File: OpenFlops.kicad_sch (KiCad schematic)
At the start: 89 parts, among them J99 OSHW_LOGO, P1 FLOPPY_CONN, P2 POWER_INPUT, P3 USB_A_FEMALE, P4 PROG_PORT, P5 JUMPER_JC, P6 ENCODER_PORT, P7 DISPLAY_PORT, P8 USB_HEADER, P9 EXTERNAL_SPEAKER, Q1 BSS138, Q2 BSS138, Q3 BSS138, Q4 BSS138, Q5 BSS138, Q6 BSS138, Q7 MMBT3904, U1 74HCT04, U3 STM32F105RBT6, U4 LM1117-3.3, Y1 8 MHz

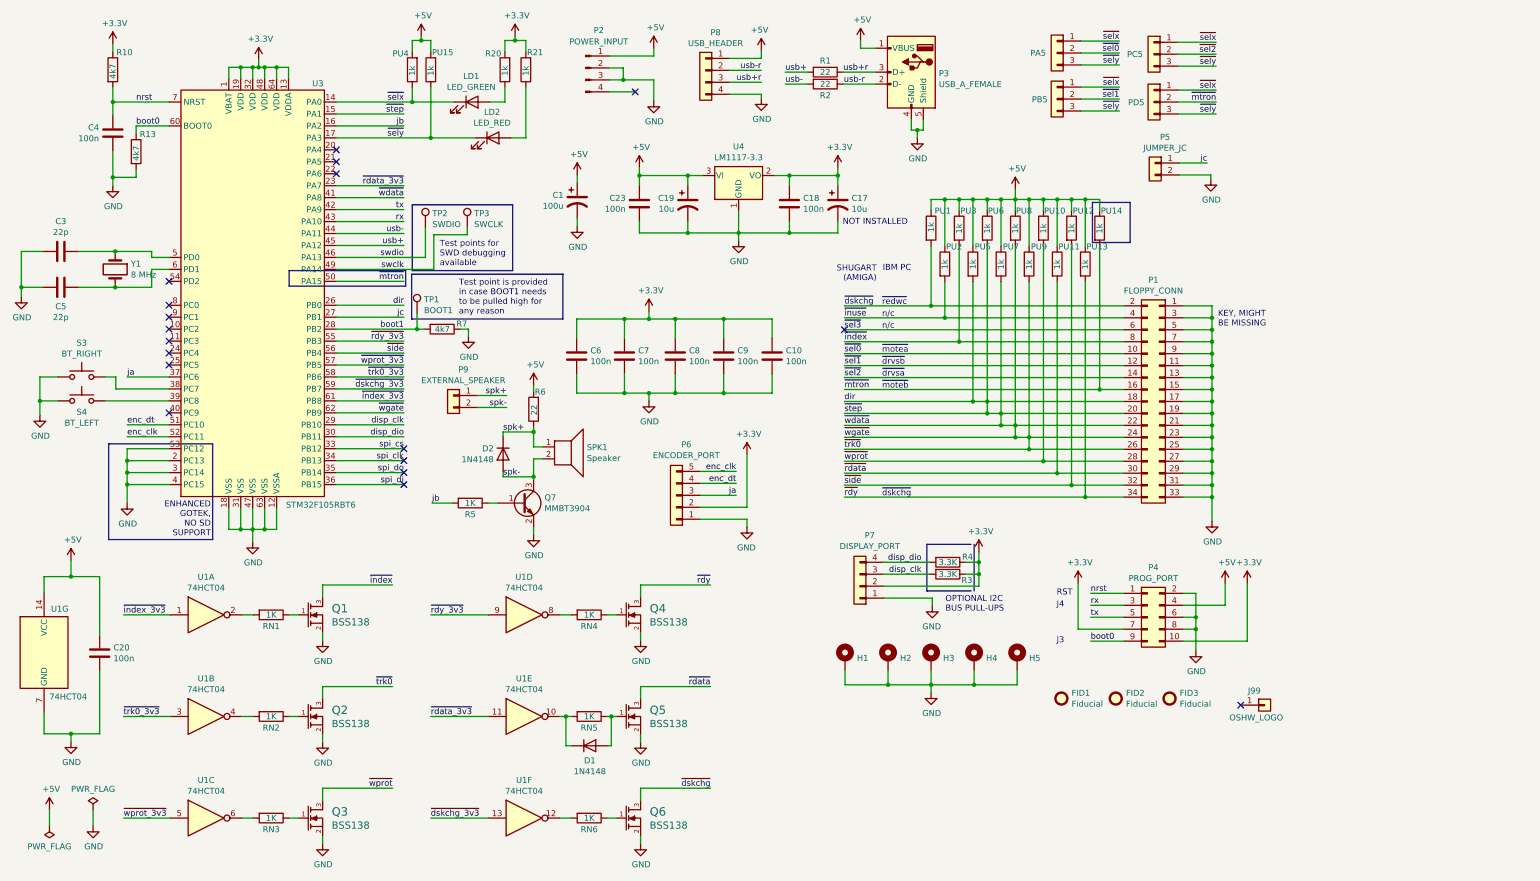
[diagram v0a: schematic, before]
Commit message: update for citizen w1d
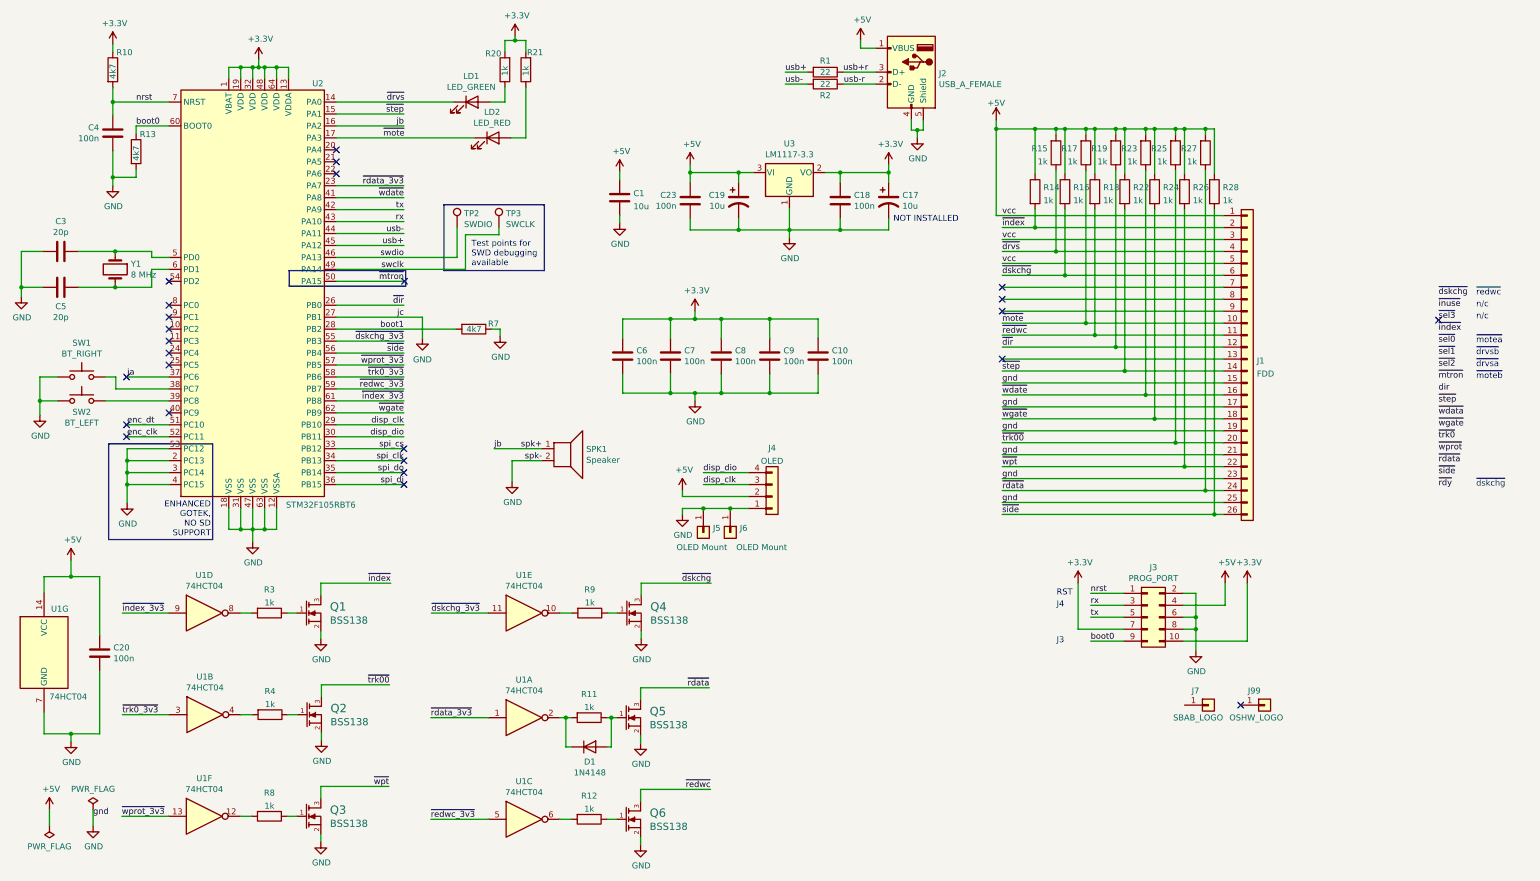
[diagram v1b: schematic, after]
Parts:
- removed C1: 100u, Capacitor_THT:CP_Radial_D6.3mm_P2.50mm, symbol Device:CP1
- removed D2: 1N4148, Diode_SMD:D_SOD-323_HandSoldering, symbol Device:D
- removed FID1, FID2, FID3: Fiducial, Fiducial:Fiducial_0.75mm_Mask1.5mm, symbol Mechanical:Fiducial
- removed H1, H2, H3, H4, H5: MountingHole_Pad, OpenFlops:MountingHole_M3_Pad, symbol Mechanical:MountingHole_Pad
- removed P1: FLOPPY_CONN, Connector_PinHeader_2.54mm:PinHeader_2x17_P2.54mm_Vertical, symbol Connector_Generic:Conn_02x17_Odd_Even
- removed P2: POWER_INPUT, OpenFlops:PinHeader_1x04_P2.54mm_Vertical, symbol Connector:Conn_01x04_Male
- removed P5: JUMPER_JC, OpenFlops:PinHeader_1x02_P2.54mm_Vertical, symbol Connector_Generic:Conn_01x02
- removed P6: ENCODER_PORT, OpenFlops:PinHeader_1x05_P2.54mm_Vertical, symbol Connector_Generic:Conn_01x05
- removed P7: DISPLAY_PORT, OpenFlops:PinHeader_1x04_P2.54mm_Vertical, symbol Connector_Generic:Conn_01x04
- removed P8: USB_HEADER, OpenFlops:PinHeader_1x04_P2.54mm_Vertical, symbol Connector_Generic:Conn_01x04
- removed P9: EXTERNAL_SPEAKER, OpenFlops:PinHeader_1x02_P2.54mm_Mute, symbol Connector_Generic:Conn_01x02
- removed PA5, PB5, PC5, PD5: Conn_01x03, OpenFlops:PinHeader_1x03_P2.54mm_Mute, symbol Connector_Generic:Conn_01x03
- removed PU1, PU10, PU11, PU12, PU13, PU14, PU15, PU2, PU3, PU4, PU5, PU6, PU7, PU8, PU9: 1k, Resistor_SMD:R_0805_2012Metric_Pad1.15x1.40mm_HandSolder, symbol Device:R
- removed Q7: MMBT3904, Package_TO_SOT_SMD:SOT-23_Handsoldering, symbol Transistor_BJT:MMBT3904
- removed R5, RN1, RN2, RN3, RN4, RN5, RN6: 1K, Resistor_SMD:R_0805_2012Metric_Pad1.15x1.40mm_HandSolder, symbol Device:R
- removed R6: 22, Resistor_SMD:R_0805_2012Metric_Pad1.15x1.40mm_HandSolder, symbol Device:R
- removed TP1: BOOT1, TestPoint:TestPoint_Pad_D1.0mm, symbol Connector:TestPoint
- added C1: 10u, Capacitor_SMD:C_0805_2012Metric_Pad1.18x1.45mm_HandSolder, symbol Device:C
- added J1: FDD, Silvestron Components:Adam_Tech_PCB-C5-26-SA-SMT_1x26_P1.00mm_Horizontal, symbol Connector_Generic:Conn_01x26
- added J4: OLED, Connector_PinHeader_2.54mm:PinHeader_1x04_P2.54mm_Vertical, symbol Connector_Generic:Conn_01x04
- added J5, J6: OLED Mount, TestPoint:TestPoint_Pad_4.0x4.0mm, symbol Connector_Generic:Conn_01x01
- added J7: SBAB_LOGO, Silvestron Components:sbab-tiny-logo, symbol Connector_Generic:Conn_01x01
- added R11, R12, R14, R15, R16, R17, R18, R19, R22, R23, R24, R25, R26, R27, R28, R8, R9: 1k, Resistor_SMD:R_0805_2012Metric_Pad1.20x1.40mm_HandSolder, symbol Device:R
- C10, C18, C20, C23, C4, C6, C7, C8, C9: footprint Capacitor_SMD:C_0805_2012Metric_Pad1.15x1.40mm_HandSolder -> Capacitor_SMD:C_0805_2012Metric_Pad1.18x1.45mm_HandSolder
- C17, C19: footprint Capacitor_THT:CP_Radial_D6.3mm_P2.50mm -> Capacitor_SMD:CP_Elec_4x5.4
- C3, C5: value 22p -> 20p; footprint Capacitor_SMD:C_0805_2012Metric_Pad1.15x1.40mm_HandSolder -> Capacitor_SMD:C_0805_2012Metric_Pad1.18x1.45mm_HandSolder; JLCPCB PN CL21C220JBANNNC -> CC0805KRX7R9BB221; LCSC (none) -> C107145; MFG Name SAMSUNG ELECTRO-MECHANICS -> YAGEO
- LD1, LD2: footprint LED_THT:LED_D3.0mm -> LED_THT:LED_D3.0mm_Horizontal_O3.81mm_Z6.0mm
- R1, R10, R13, R2, R20, R21, R7: footprint Resistor_SMD:R_0805_2012Metric_Pad1.15x1.40mm_HandSolder -> Resistor_SMD:R_0805_2012Metric_Pad1.20x1.40mm_HandSolder
- R3, R4: value 3.3K -> 1k; footprint Resistor_SMD:R_0805_2012Metric_Pad1.15x1.40mm_HandSolder -> Resistor_SMD:R_0805_2012Metric_Pad1.20x1.40mm_HandSolder
- SPK1: footprint OpenFlops:Buzzer -> Buzzer_Beeper:Buzzer_CUI_CPT-9019S-SMT
- SW1: renamed from S3; footprint OpenFlops:PUSH_BUTTON_RIGHT_ANGLE -> Button_Switch_THT:SW_Tactile_SPST_Angled_PTS645Vx83-2LFS
- SW2: renamed from S4; footprint OpenFlops:PUSH_BUTTON_RIGHT_ANGLE -> Button_Switch_THT:SW_Tactile_SPST_Angled_PTS645Vx83-2LFS
- U2: renamed from U3; footprint OpenFlops:LQFP-64_Handsoldering -> Package_QFP:LQFP-64_10x10mm_P0.5mm
- Y1: footprint OpenFlops:Crystal_HC49-DualType -> Crystal:Crystal_SMD_5032-2Pin_5.0x3.2mm_HandSoldering
- renumbered P3 to J2, P4 to J3, U4 to U3
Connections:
- net jc is gone; now on net GND: U2.27 (PB1)
- net spk+ is gone; now on net jb: SPK1.1
- net spk- is gone; now on net GND: SPK1.2
- net +3V3: no longer R3.1, R4.1
- net +5V: now also C1.1, J1.1 (Pin_1), J1.3 (Pin_3), J1.5 (Pin_5), J4.2 (Pin_2), R14.1, R15.2, R16.1, R17.2, R18.1, R19.2, R22.1, R23.2, R24.1, R25.2, R26.1, R27.2, R28.1
- net GND: now also C1.2, J1.15 (Pin_15), J1.17 (Pin_17), J1.19 (Pin_19), J1.21 (Pin_21), J1.23 (Pin_23), J1.25 (Pin_25), J4.1 (Pin_1), J5.1 (Pin_1), J6.1 (Pin_1)
- net dir: no longer Q2.3 (D), U2.15 (PA1), U2.26 (PB0), U2.41 (PA8), U2.62 (PB9)
- net disp_clk: now also J4.3 (Pin_3); no longer R3.2
- net disp_dio: now also J4.4 (Pin_4); no longer R4.2
- net ~{dskchg_3v3}: now also U1.11, U2.55 (PB3); no longer U1.13, U2.59 (PB7)
- net ~{dskchg}: now also Q4.3 (D), J1.6 (Pin_6), R16.2; no longer Q6.3 (D)
- net ~{index_3v3}: now also U1.9; no longer U1.1
- net ~{index}: now also J1.2 (Pin_2), R14.2
- net ~{rdata_3v3}: now also U1.1; no longer U1.11
- net ~{rdata}: now also J1.24 (Pin_24), R27.1
- net ~{rdy}: no longer Q4.3 (D)
- net ~{side}: now also J1.26 (Pin_26), R28.2
- net ~{wprot_3v3}: now also U1.13; no longer U1.5
- net ~{wprot}: no longer Q3.3 (D)
- net at U1.2: now also D1.1 (K), R11.2
- net at U1.4: now also R4.2
- net at U1.6: now also R12.2
- net at U1.8: now also R3.2
- net at U1.10: now also R9.2; no longer D1.1 (K)
- net at U1.12: now also R8.2
- net at Q1.1 (G): now also R3.1
- net at Q2.1 (G): now also R4.1
- net at Q3.1 (G): now also R8.1
- net at Q4.1 (G): now also R9.1
- net at D1.2 (A), Q5.1 (G): now also R11.1
- net at Q6.1 (G): now also R12.1
- removed net ~{rdy_3v3}: U1.9, U2.55 (PB3)
- net ~{selx} renamed ~{drvs}
- net ~{drvs}: now also J1.4 (Pin_4), R15.1
- net ~{sely} renamed ~{mote}
- net ~{mote}: now also J1.10 (Pin_10), R17.1
- new net ~{dir}: J1.12 (Pin_12), R19.1, U2.26 (PB0)
- new net ~{redwc_3v3}: U1.5, U2.59 (PB7)
- new net ~{redwc}: J1.11 (Pin_11), Q6.3 (D), R18.2
- new net ~{step}: J1.14 (Pin_14), R22.2, U2.15 (PA1)
- new net ~{trk00}: J1.20 (Pin_20), Q2.3 (D), R25.1
- new net ~{wdate}: J1.16 (Pin_16), R23.1, U2.41 (PA8)
- new net ~{wgate}: J1.18 (Pin_18), R24.2, U2.62 (PB9)
- new net ~{wpt}: J1.22 (Pin_22), Q3.3 (D), R26.2
- no-connect marks 18 -> 25
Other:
- note removed: "IBM PC"
- note removed: "KEY, MIGHT BE MISSING"
- note removed: "OPTIONAL I2C BUS PULL-UPS"
- note removed: "SHUGART (AMIGA)"
- note removed: "Test point is provided in case BOOT1 needs to be pulled high for any reason"
- moved on the sheet: C10, C17, C18, C19, C23, C6, C7, C8, C9, Q1, Q3, R7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

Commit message: rev 10; more smd for more assembly
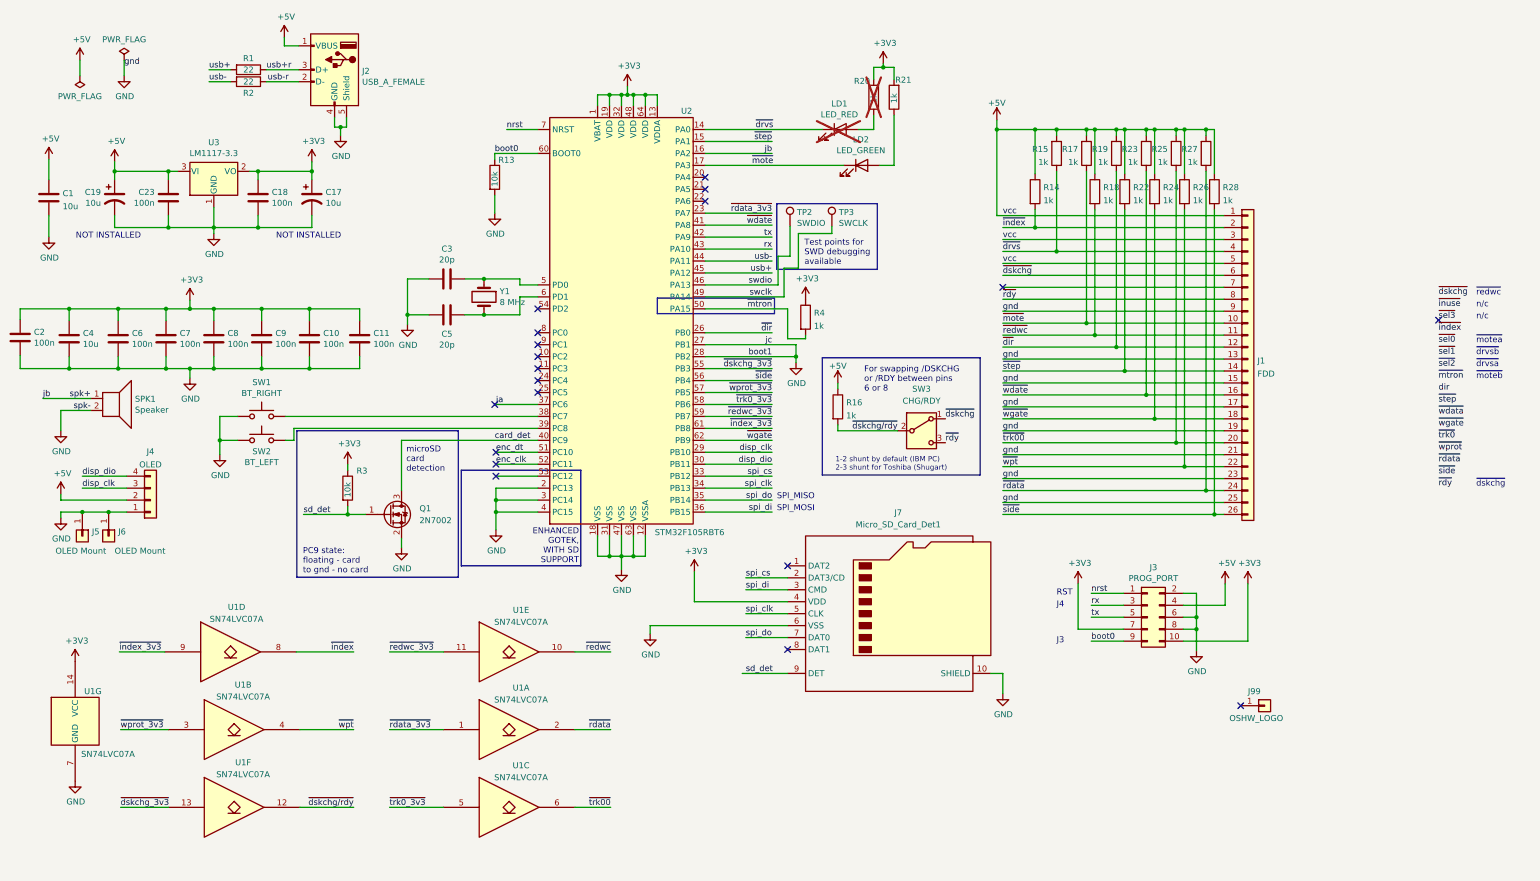
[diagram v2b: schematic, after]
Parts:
- removed C20: 100n, Capacitor_SMD:C_0805_2012Metric_Pad1.18x1.45mm_HandSolder, symbol Device:C
- removed D1: 1N4148, Diode_SMD:D_SOD-323_HandSoldering, symbol Device:D
- removed J7: SBAB_LOGO, Silvestron Components:sbab-tiny-logo, symbol Connector_Generic:Conn_01x01
- removed Q1, Q2, Q3, Q4, Q5, Q6: BSS138, Package_TO_SOT_SMD:SOT-23_Handsoldering, symbol w_transistor:MOS_N_GSD
- removed R10, R7: 4k7, Resistor_SMD:R_0805_2012Metric_Pad1.20x1.40mm_HandSolder, symbol Device:R
- removed R11, R12, R8, R9: 1k, Resistor_SMD:R_0805_2012Metric_Pad1.20x1.40mm_HandSolder, symbol Device:R
- removed U1: 74HCT04, Package_SO:SOIC-14_3.9x8.7mm_P1.27mm, symbol 74xx:74HC04
- added C11, C2: 100n, Capacitor_SMD:C_0805_2012Metric_Pad1.18x1.45mm_HandSolder, symbol Device:C
- added J7: Micro_SD_Card_Det1, Silvestron Components:microSD_XUNPU_TF-114, symbol Connector:Micro_SD_Card_Det1
- added Q1: 2N7002, Package_TO_SOT_SMD:SOT-23, symbol Transistor_FET:2N7002
- added SW3: CHG/RDY, Button_Switch_SMD:SW_SPDT_PCM12, symbol Switch:SW_SPDT
- added U1: SN74LVC07A, Package_SO:TSSOP-14_4.4x5mm_P0.65mm, symbol Silvestron Components:SN74LVC07A
- C1: LCSC (none) -> C15850
- C3, C5: LCSC C107145 -> C1798
- C4: value 100n -> 10u; JLCPCB PN CC0805KRX7R9BB104 -> (none); LCSC (none) -> C15850; MFG Name YAGEO -> (none); MFG Part Num MULTILAYER CERAMIC CAPACITORS MLCC - SMD/SMT 100NF 50V 0805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 -> (none)
- J1: LCSC (none) -> C19188849
- J2: footprint OpenFlops:USB_A_FEMALE -> Connector_USB:USB_A_Receptacle_GCT_USB1046; LCSC (none) -> C42637
- LD1: value LED_GREEN -> LED_RED; footprint LED_THT:LED_D3.0mm_Horizontal_O3.81mm_Z6.0mm -> LED_SMD:LED_0805_2012Metric; now not fitted
- LD2: value LED_RED -> LED_GREEN; footprint LED_THT:LED_D3.0mm_Horizontal_O3.81mm_Z6.0mm -> LED_SMD:LED_0805_2012Metric; LCSC (none) -> C2297
- R1: LCSC (none) -> C17561
- R13: value 4k7 -> 10k; JLCPCB PN 0805W8F4701T5E -> (none); MFG Name UNIROYAL ELEC -> (none); MFG Part Num CHIP RESISTOR - SURFACE MOUNT 4.7KOHMS ±1% 1/8W 0805 ROHS -> (none)
- R14, R4: LCSC (none) -> C17513
- R20: now not fitted
- R3: value 1k -> 10k; LCSC (none) -> C17414
- SPK1: LCSC (none) -> C968734
- SW2: LCSC (none) -> C125034
- U2: LCSC (none) -> C8349
- U3: LCSC (none) -> C6186
- Y1: LCSC (none) -> C115962
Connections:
- net boot1 is gone; now on net GND: U2.28 (PB2)
- net +3V3: now also C4.1, R3.1, R4.1, C11.1, C2.1, J7.4 (VDD), U1.14 (VCC)
- net GND: now also J1.13 (Pin_13), J1.9 (Pin_9), C11.2, C2.2, J7.10 (SHIELD), J7.6 (VSS), Q1.2 (S), U1.7 (GND); no longer U2.53 (PC12)
- net nrst: no longer C4.1
- net spi_clk: now also J7.5 (CLK)
- net spi_cs: now also J7.2 (DAT3/CD)
- net spi_di: now also J7.3 (CMD)
- net spi_do: now also J7.7 (DAT0)
- net ~{dskchg_3v3}: now also U1.13
- net ~{dskchg}: now also SW3.1 (A); no longer R16.2
- net ~{index_3v3}: now also U1.9
- net ~{index}: now also U1.8
- net ~{mtron}: now also R4.2
- net ~{rdata_3v3}: now also U1.1
- net ~{rdata}: now also U1.2
- net ~{rdy}: now also J1.8 (Pin_8), SW3.3 (C)
- net ~{redwc_3v3}: now also U1.11
- net ~{redwc}: now also U1.10
- net ~{trk00}: now also U1.6
- net ~{trk0_3v3}: now also U1.5
- net ~{wprot_3v3}: now also U1.3
- net ~{wpt}: now also U1.4
- net card_det: now reaches U2.40 (PC9)
- net card_det: now also Q1.3 (D)
- net sd_det: now reaches R3.2
- net sd_det: now also J7.9 (DET), Q1.1 (G)
- new net ~{dskchg/rdy}: R16.2, SW3.2 (B), U1.12
- no-connect marks 25 -> 19
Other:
- note added: "1-2 shunt by default (IBM PC) 2-3 shunt for Toshiba (Shugart)"
- note added: "ENHANCED GOTEK, WITH SD SUPPORT"
- note added: "For swapping /DSKCHG or /RDY between pins 6 or 8"
- note added: "PC9 state: floating - card to gnd - no card"
- note added: "SPI_MISO"
- note added: "SPI_MOSI"
- note added: "microSD card detection"
- note removed: "ENHANCED GOTEK, NO SD SUPPORT"
- moved on the sheet: C1, C10, C17, C18, C19, C23, C3, C5, C6, C7, C8, C9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

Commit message: rev 11; fixed issue with usb port being too far forward
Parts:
- J2: footprint Connector_USB:USB_A_Receptacle_GCT_USB1046 -> Connector_USB:USB_A_TE_292303-7_Horizontal; LCSC C42637 -> C2763369
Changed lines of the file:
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@@
 			)
 		)
-		(property "Footprint" "Connector_USB:USB_A_Receptacle_GCT_USB1046"
+		(property "Footprint" "Connector_USB:USB_A_TE_292303-7_Horizontal"
 			(at 78.486 27.432 0)
 			(effects
@@
 			)
 		)
-		(property "LCSC" "C42637"
+		(property "LCSC" "C2763369"
 			(at 82.296 26.162 0)
 			(effects
